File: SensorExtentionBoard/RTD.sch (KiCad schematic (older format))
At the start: 108 parts, among them J10 Conn_01x02_Male, J11 Conn_01x02_Male, Q1 AOD508, Q10 AOD508, Q11 AOD508, Q12 AOD508, Q13 AOD508, Q14 AOD508, Q15 AOD508, Q16 AOD508, Q17 AOD508, Q18 AOD508, Q19 AOD508, Q2 AOD508, Q20 AOD508, Q21 AOD508, Q22 AOD508, Q23 AOD508, Q24 AOD508, Q25 AOD508, Q26 AOD508, Q27 AOD508, Q28 AOD508, Q29 AOD508, Q3 AOD508, Q30 AOD508, Q4 AOD508, Q5 AOD508, Q6 AOD508, Q7 AOD508, Q8 AOD508, Q9 AOD508, U7 TCA9555DBR, U8 TCA9555DBR

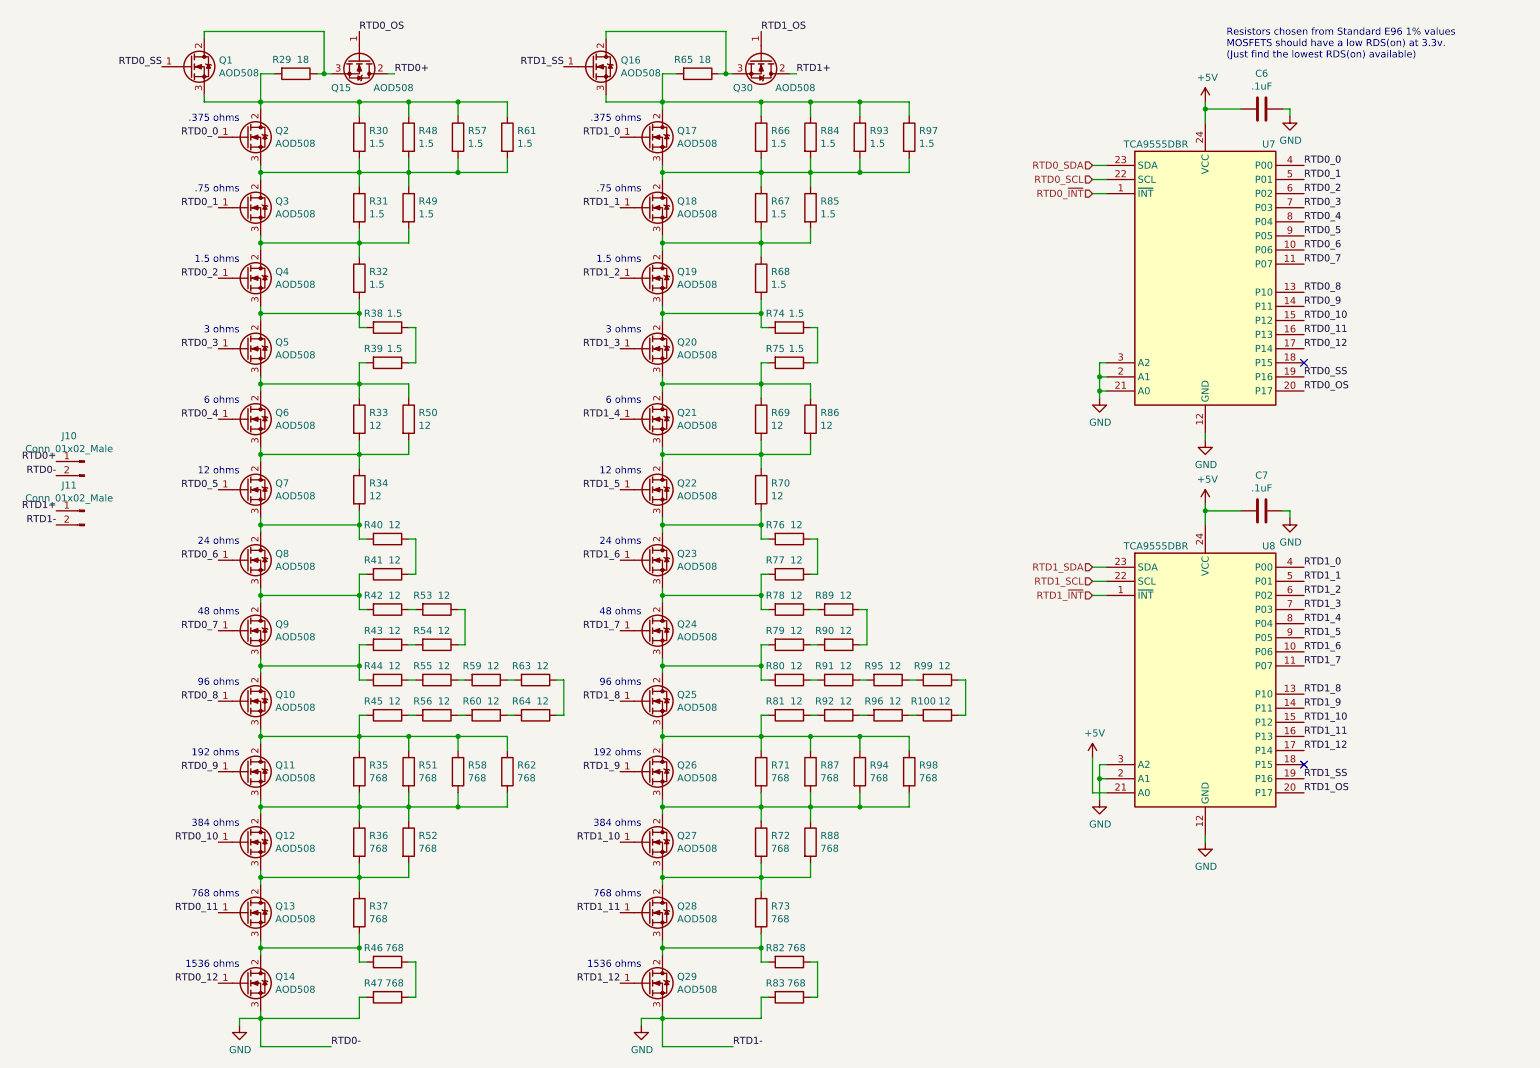
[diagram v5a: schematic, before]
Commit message: Replaced ADS1115 with ADS1015 on PT page
The ADS1115 is being used to read the voltages provided by the Helix
system to the pressure transducers. The ADS1015 is already doing
the same job for the Hall Effect sensors, however the ADS1015 has
4 bits lower accuracy. High accuracy is not needed for this
application so be replacing the ADS1115 with the ADS1015 we can
reduce cost and more importantly reduce BOM size making the project
logistics easier to manage.
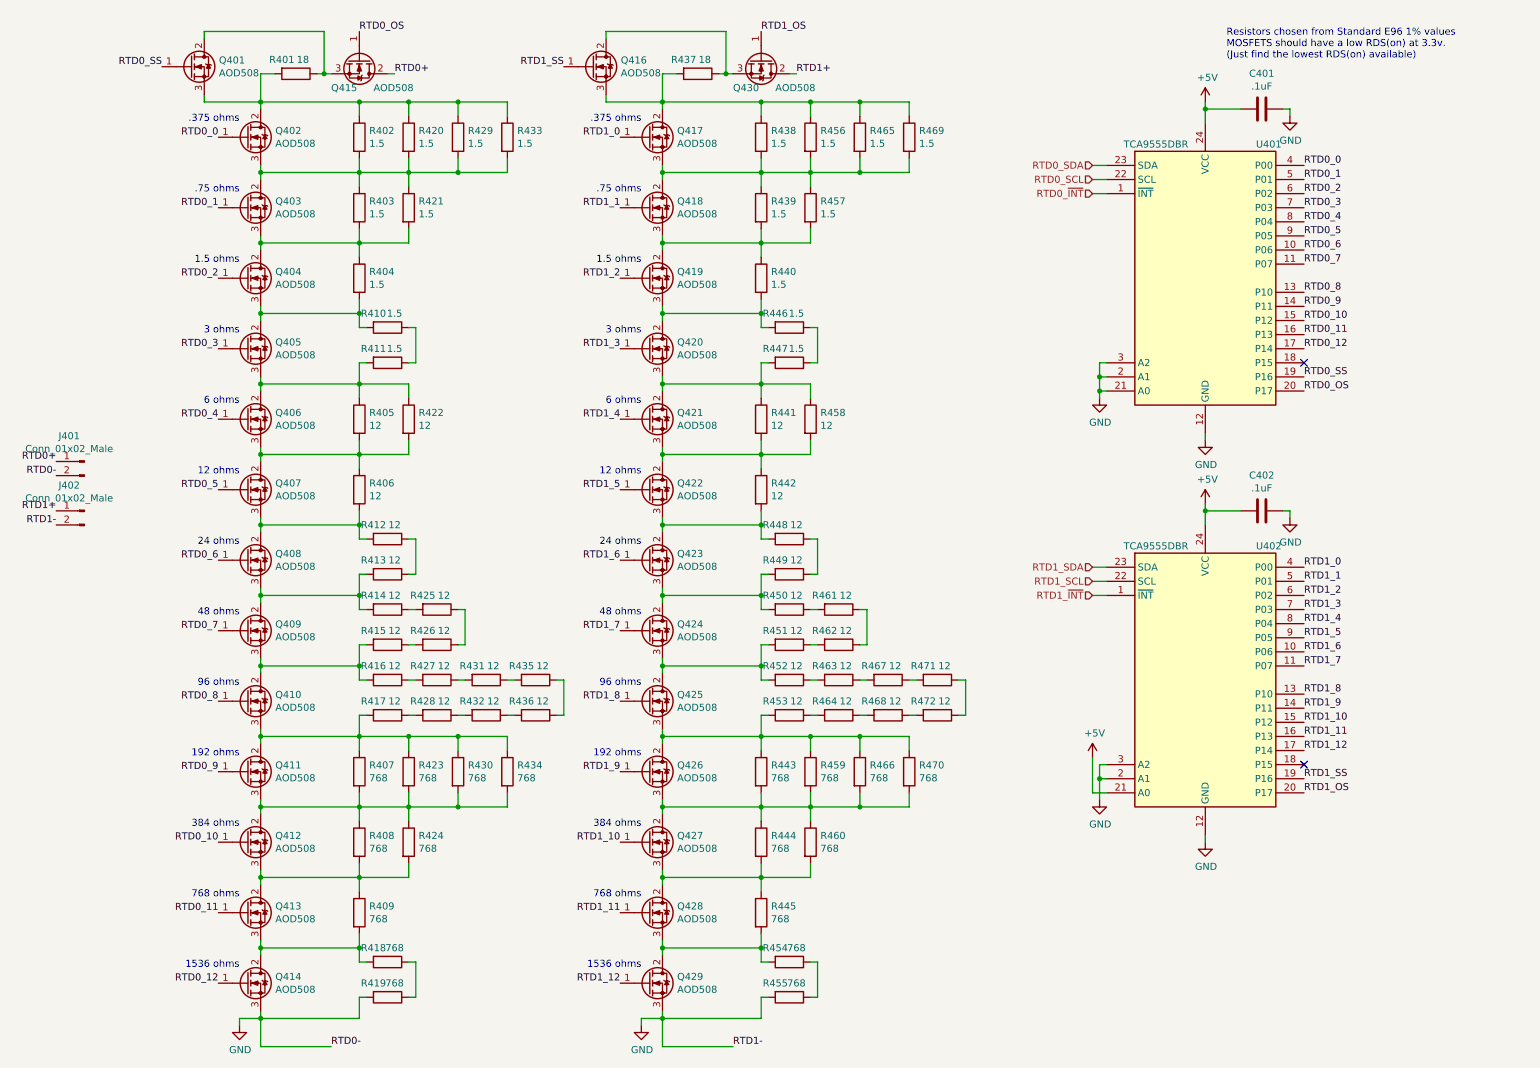
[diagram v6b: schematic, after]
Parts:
- renumbered C6 to C401, C7 to C402, J10 to J401, J11 to J402, Q1 to Q401, Q2 to Q402, Q3 to Q403, Q4 to Q404, Q5 to Q405, Q6 to Q406, Q7 to Q407, Q8 to Q408, Q9 to Q409, Q10 to Q410, Q11 to Q411, Q12 to Q412, Q13 to Q413, Q14 to Q414, Q15 to Q415, Q16 to Q416, Q17 to Q417, Q18 to Q418, Q19 to Q419, Q20 to Q420, Q21 to Q421, Q22 to Q422, Q23 to Q423, Q24 to Q424, Q25 to Q425, Q26 to Q426, Q27 to Q427, Q28 to Q428, Q29 to Q429, Q30 to Q430, R29 to R401, R30 to R402, R31 to R403, R32 to R404, R33 to R405, R34 to R406, R35 to R407, R36 to R408, R37 to R409, R38 to R410, R39 to R411, R40 to R412, R41 to R413, R42 to R414, R43 to R415, R44 to R416, R45 to R417, R46 to R418, R47 to R419, R48 to R420, R49 to R421, R50 to R422, R51 to R423, R52 to R424, R53 to R425, R54 to R426, R55 to R427, R56 to R428, R57 to R429, R58 to R430, R59 to R431, R60 to R432, R61 to R433, R62 to R434, R63 to R435, R64 to R436, R65 to R437, R66 to R438, R67 to R439, R68 to R440, R69 to R441, R70 to R442, R71 to R443, R72 to R444, R73 to R445, R74 to R446, R75 to R447, R76 to R448, R77 to R449, R78 to R450, R79 to R451, R80 to R452, R81 to R453, R82 to R454, R83 to R455, R84 to R456, R85 to R457, R86 to R458, R87 to R459, R88 to R460, R89 to R461, R90 to R462, R91 to R463, R92 to R464, R93 to R465, R94 to R466, R95 to R467, R96 to R468, R97 to R469, R98 to R470, R99 to R471, R100 to R472, U7 to U401, U8 to U402

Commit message: Added header for programming the EEPROM memory on the SEB
Adding this header may allow the test rig to load new memory configs
onto the SEB under test prior to running tests. This will allow
greater ability for automation of testing when the new software
requires a change to the config onboard the SEB.
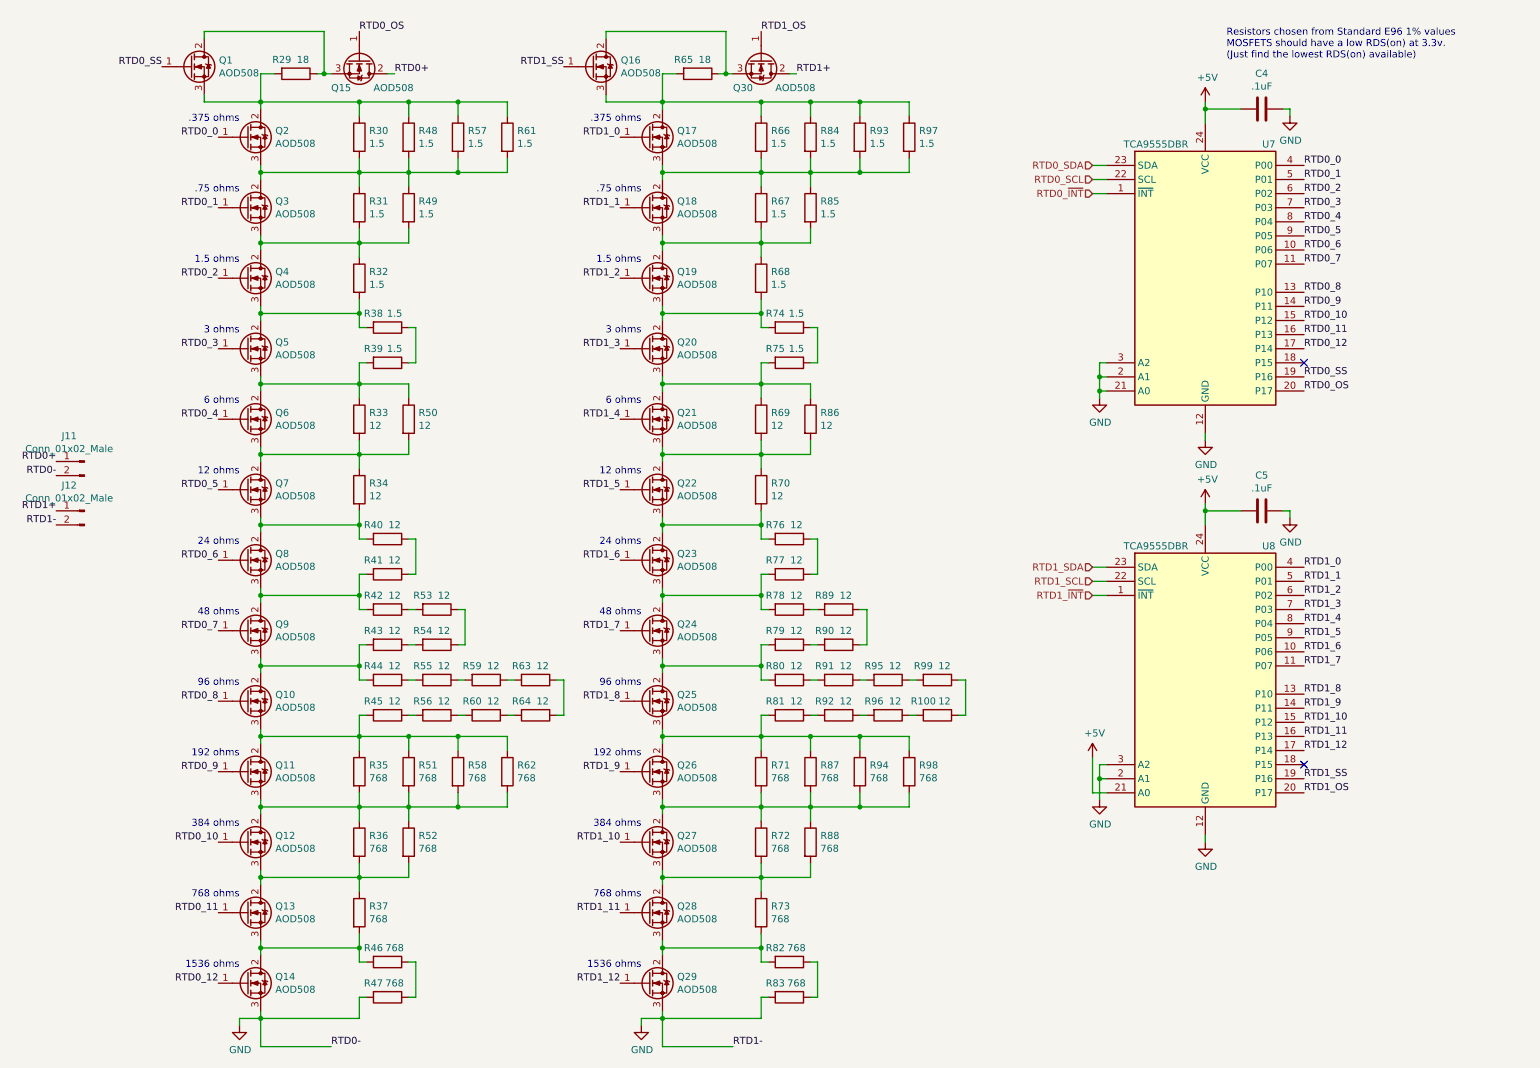
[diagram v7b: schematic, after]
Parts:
- renumbered C401 to C4, C402 to C5, J401 to J11, J402 to J12, Q401 to Q1, Q410 to Q10, Q411 to Q11, Q412 to Q12, Q413 to Q13, Q414 to Q14, Q415 to Q15, Q416 to Q16, Q417 to Q17, Q418 to Q18, Q419 to Q19, Q402 to Q2, Q420 to Q20, Q421 to Q21, Q422 to Q22, Q423 to Q23, Q424 to Q24, Q425 to Q25, Q426 to Q26, Q427 to Q27, Q428 to Q28, Q429 to Q29, Q403 to Q3, Q430 to Q30, Q404 to Q4, Q405 to Q5, Q406 to Q6, Q407 to Q7, Q408 to Q8, Q409 to Q9, R472 to R100, R401 to R29, R402 to R30, R403 to R31, R404 to R32, R405 to R33, R406 to R34, R407 to R35, R408 to R36, R409 to R37, R410 to R38, R411 to R39, R412 to R40, R413 to R41, R414 to R42, R415 to R43, R416 to R44, R417 to R45, R418 to R46, R419 to R47, R420 to R48, R421 to R49, R422 to R50, R423 to R51, R424 to R52, R425 to R53, R426 to R54, R427 to R55, R428 to R56, R429 to R57, R430 to R58, R431 to R59, R432 to R60, R433 to R61, R434 to R62, R435 to R63, R436 to R64, R437 to R65, R438 to R66, R439 to R67, R440 to R68, R441 to R69, R442 to R70, R443 to R71, R444 to R72, R445 to R73, R446 to R74, R447 to R75, R448 to R76, R449 to R77, R450 to R78, R451 to R79, R452 to R80, R453 to R81, R454 to R82, R455 to R83, R456 to R84, R457 to R85, R458 to R86, R459 to R87, R460 to R88, R461 to R89, R462 to R90, R463 to R91, R464 to R92, R465 to R93, R466 to R94, R467 to R95, R468 to R96, R469 to R97, R470 to R98, R471 to R99, U401 to U7, U402 to U8

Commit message: Changed component footprints to conform to RP standard components
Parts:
- C4, C5: footprint (none) -> Capacitor_SMD:C_1206_3216Metric_Pad1.42x1.75mm_HandSolder
- J11, J12: footprint Connector_Molex:Molex_MicroClasp_55932-0210_1x02_P2.00mm_Vertical -> Connector_Molex:Molex_MicroClasp_55932-0230_1x02_P2.00mm_Vertical
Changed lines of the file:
@@
 encoding utf-8
 Sheet 4 5
-Title ""
-Date ""
-Rev ""
-Comp ""
-Comment1 ""
+Title "Helix Test Rig SEB"
+Date "2020-01-14"
+Rev "1.0.0"
+Comp "SDSU Rocket Project"
+Comment1 "Schematic Design: David Knight"
 Comment2 ""
 Comment3 ""
@@
 NoConn ~ 9700 5750
 $Comp
-L power:GND #PWR046
+L power:GND #PWR049
 U 1 1 5E9AA3EC
 P 9000 6300
-F 0 "#PWR046" H 9000 6050 50  0001 C CNN
+F 0 "#PWR049" H 9000 6050 50  0001 C CNN
 F 1 "GND" H 9005 6127 50  0000 C CNN
 F 2 "" H 9000 6300 50  0001 C CNN
@@
 	9000 6300 9000 6250
 $Comp
-L power:GND #PWR044
+L power:GND #PWR047
 U 1 1 5E9D2908
 P 9000 3450
-F 0 "#PWR044" H 9000 3200 50  0001 C CNN
+F 0 "#PWR047" H 9000 3200 50  0001 C CNN
 F 1 "GND" H 9005 3277 50  0000 C CNN
 F 2 "" H 9000 3450 50  0001 C CNN
@@
 	9000 3450 9000 3400
 $Comp
-L power:+5V #PWR043
+L power:+5V #PWR046
 U 1 1 5E9ED07C
 P 9000 1050
-F 0 "#PWR043" H 9000 900 50  0001 C CNN
+F 0 "#PWR046" H 9000 900 50  0001 C CNN
 F 1 "+5V" H 9015 1223 50  0000 C CNN
 F 2 "" H 9000 1050 50  0001 C CNN
@@
 	9000 1050 9000 1100
 $Comp
-L power:+5V #PWR045
+L power:+5V #PWR048
 U 1 1 5EA01291
 P 9000 3900
-F 0 "#PWR045" H 9000 3750 50  0001 C CNN
+F 0 "#PWR048" H 9000 3750 50  0001 C CNN
 F 1 "+5V" H 9015 4073 50  0000 C CNN
 F 2 "" H 9000 3900 50  0001 C CNN
@@
 	9000 3900 9000 3950
 $Comp
-L power:GND #PWR041
+L power:GND #PWR044
 U 1 1 5EA15395
 P 8250 3150
-F 0 "#PWR041" H 8250 2900 50  0001 C CNN
+F 0 "#PWR044" H 8250 2900 50  0001 C CNN
 F 1 "GND" H 8255 2977 50  0000 C CNN
 F 2 "" H 8250 3150 50  0001 C CNN
@@
 	8250 3100 8250 3000
 $Comp
-L power:GND #PWR042
+L power:GND #PWR045
 U 1 1 5EA526F6
 P 8250 6000
-F 0 "#PWR042" H 8250 5750 50  0001 C CNN
+F 0 "#PWR045" H 8250 5750 50  0001 C CNN
 F 1 "GND" H 8255 5827 50  0000 C CNN
 F 2 "" H 8250 6000 50  0001 C CNN
@@
 	8200 5950 8200 5700
 $Comp
-L power:+5V #PWR040
+L power:+5V #PWR043
 U 1 1 5EA7E02B
 P 8200 5700
-F 0 "#PWR040" H 8200 5550 50  0001 C CNN
+F 0 "#PWR043" H 8200 5550 50  0001 C CNN
 F 1 "+5V" H 8215 5873 50  0000 C CNN
 F 2 "" H 8200 5700 50  0001 C CNN
@@
 F 0 "J11" H 1158 3781 50  0000 C CNN
 F 1 "Conn_01x02_Male" H 1158 3690 50  0000 C CNN
-F 2 "Connector_Molex:Molex_MicroClasp_55932-0210_1x02_P2.00mm_Vertical" H 1050 3600 50  0001 C CNN
+F 2 "Connector_Molex:Molex_MicroClasp_55932-0230_1x02_P2.00mm_Vertical" H 1050 3600 50  0001 C CNN
 F 3 "~" H 1050 3600 50  0001 C CNN
 	1    1050 3600
@@
 F 0 "J12" H 1158 4131 50  0000 C CNN
 F 1 "Conn_01x02_Male" H 1158 4040 50  0000 C CNN
-F 2 "Connector_Molex:Molex_MicroClasp_55932-0210_1x02_P2.00mm_Vertical" H 1050 3950 50  0001 C CNN
+F 2 "Connector_Molex:Molex_MicroClasp_55932-0230_1x02_P2.00mm_Vertical" H 1050 3950 50  0001 C CNN
 F 3 "~" H 1050 3950 50  0001 C CNN
 	1    1050 3950
@@
 F 0 "C4" V 9148 1100 50  0000 C CNN
 F 1 ".1uF" V 9239 1100 50  0000 C CNN
-F 2 "" H 9438 950 50  0001 C CNN
+F 2 "Capacitor_SMD:C_1206_3216Metric_Pad1.42x1.75mm_HandSolder" H 9438 950 50  0001 C CNN
 F 3 "~" H 9400 1100 50  0001 C CNN
 	1    9400 1100
@@
 P 9600 1150
 AR Path="/5E14F6A2" Ref="#PWR?"  Part="1"
-AR Path="/5E059E9F/5E14F6A2" Ref="#PWR047"  Part="1"
-F 0 "#PWR047" H 9600 900 50  0001 C CNN
+AR Path="/5E059E9F/5E14F6A2" Ref="#PWR050"  Part="1"
+F 0 "#PWR050" H 9600 900 50  0001 C CNN
 F 1 "GND" H 9605 977 50  0000 C CNN
 F 2 "" H 9600 1150 50  0001 C CNN
@@
 F 0 "C5" V 9148 3950 50  0000 C CNN
 F 1 ".1uF" V 9239 3950 50  0000 C CNN
-F 2 "" H 9438 3800 50  0001 C CNN
+F 2 "Capacitor_SMD:C_1206_3216Metric_Pad1.42x1.75mm_HandSolder" H 9438 3800 50  0001 C CNN
 F 3 "~" H 9400 3950 50  0001 C CNN
 	1    9400 3950
@@
 P 9600 4000
 AR Path="/5E1993DB" Ref="#PWR?"  Part="1"
-AR Path="/5E059E9F/5E1993DB" Ref="#PWR048"  Part="1"
-F 0 "#PWR048" H 9600 3750 50  0001 C CNN
+AR Path="/5E059E9F/5E1993DB" Ref="#PWR051"  Part="1"
+F 0 "#PWR051" H 9600 3750 50  0001 C CNN
 F 1 "GND" H 9605 3827 50  0000 C CNN
 F 2 "" H 9600 4000 50  0001 C CNN
@@
 	9000 3950 9000 4050
 $Comp
-L power:GND #PWR038
+L power:GND #PWR041
 U 1 1 5E1B7251
 P 2150 7600
-F 0 "#PWR038" H 2150 7350 50  0001 C CNN
+F 0 "#PWR041" H 2150 7350 50  0001 C CNN
 F 1 "GND" H 2155 7427 50  0000 C CNN
 F 2 "" H 2150 7600 50  0001 C CNN
@@
 	2150 7550 2300 7550
 $Comp
-L power:GND #PWR039
+L power:GND #PWR042
 U 1 1 5E1D1E5B
 P 5000 7600
-F 0 "#PWR039" H 5000 7350 50  0001 C CNN
+F 0 "#PWR042" H 5000 7350 50  0001 C CNN
 F 1 "GND" H 5005 7427 50  0000 C CNN
 F 2 "" H 5000 7600 50  0001 C CNN
